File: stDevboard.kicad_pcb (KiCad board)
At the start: 4 copper layers, 50 x 100 mm, 141 parts, among them IC1 MPM3610GQV-Z, IC2 IRFR9014PBF, IC6 AT25SF041B-SSHB-B, J1 battery, J10 73412-0114, J11 USB_C_Receptacle_USB2.0_16P, J12 73412-0114, J14 Micro_SD_Card_Det2, J2 USB_C_Receptacle_USB2.0_16P, J4 Screw_Terminal_01x12, Q1 DMN3404L, Q2 DMN3404L, Q3 DMN3404L, Q4 DMN3404L, Q5 DMN3404L, Q6 MMBT2222A, Q7 MMBT2222A, Q8 DMN3404L, U1 STM32U073CCUx, U2 STM32U585CIUxQ, Y1 ECS-160-8-36B2-CKM-TR, Y2 CM7V-T1A-32.768KHZ, Y3 ECS-TXO-25CSMV-320-AM-TR, Y4 CM7V-T1A-32.768KHZ

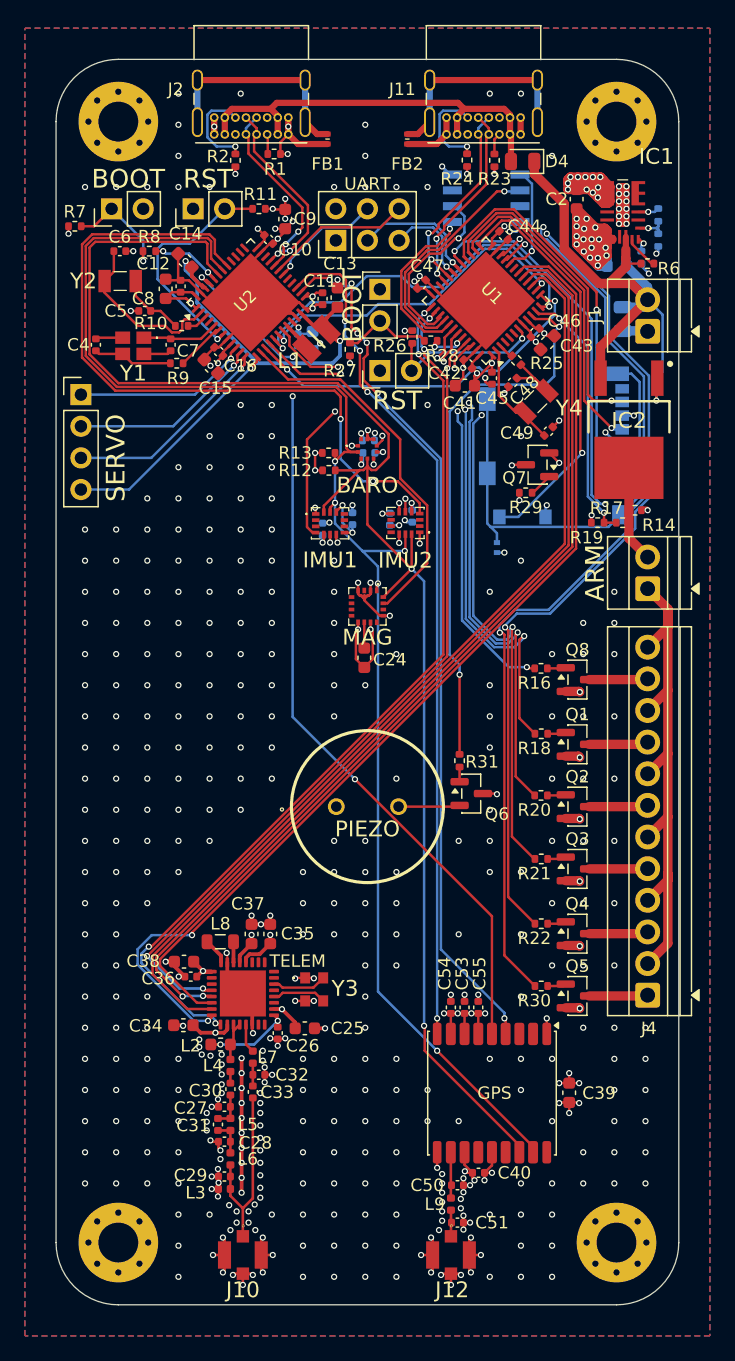
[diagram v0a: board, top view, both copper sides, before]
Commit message: schematic updated - need to redo the layout now
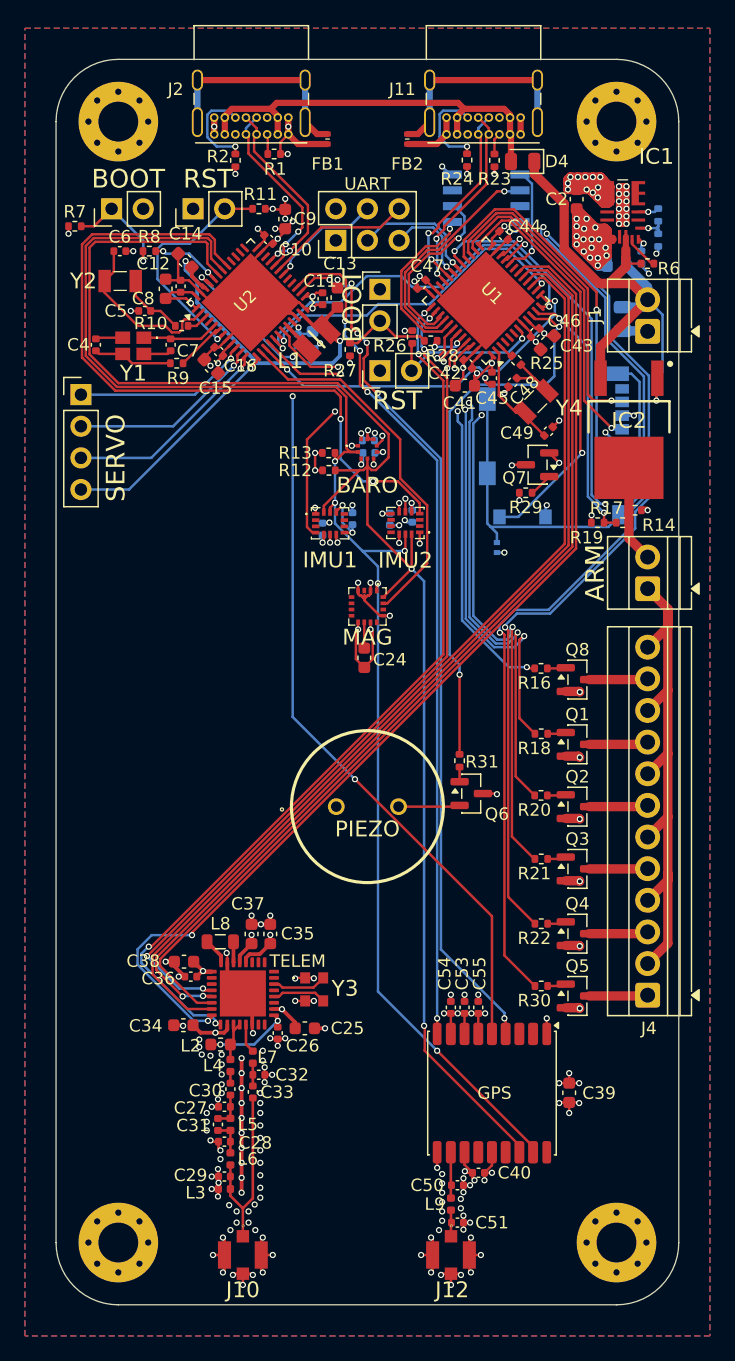
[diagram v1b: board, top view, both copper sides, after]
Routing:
- net GND: vias 471 -> 195

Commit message: started redoing layout for new pinout
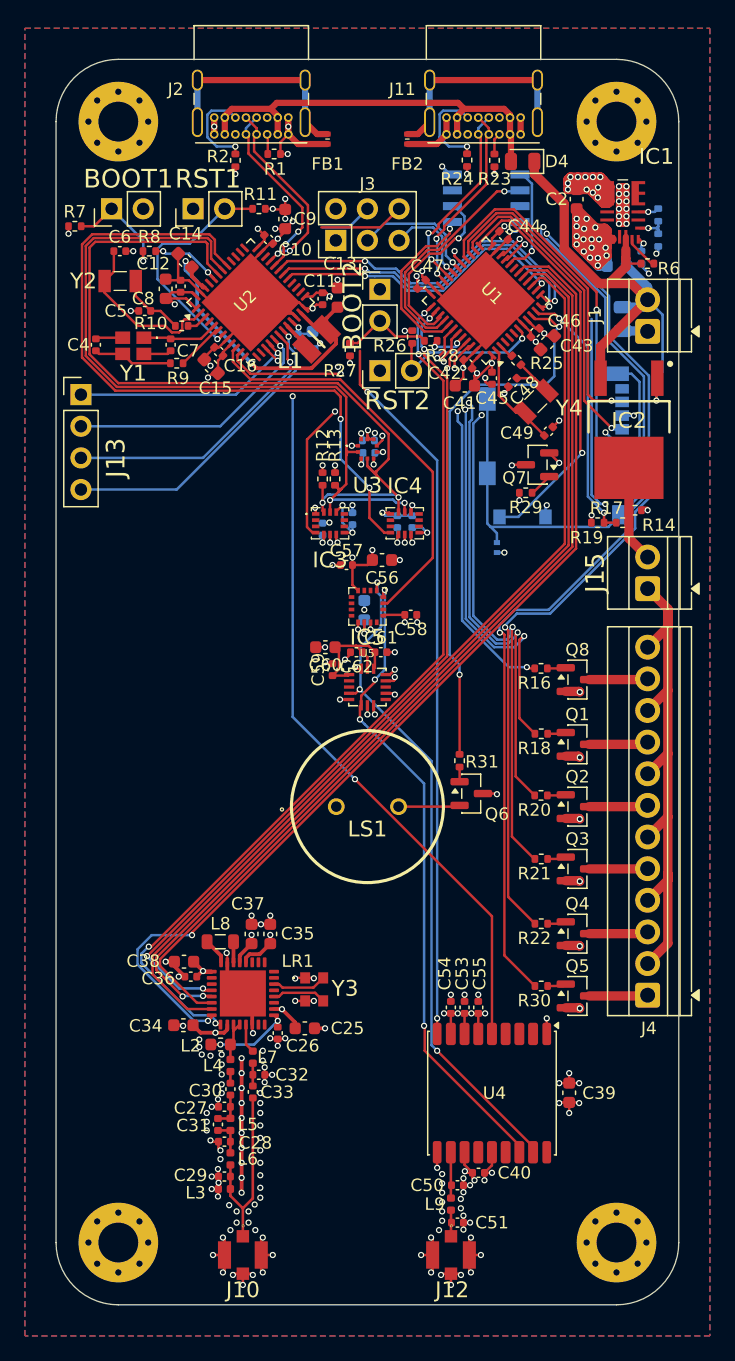
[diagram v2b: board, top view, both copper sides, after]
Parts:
- added C56: 1uF, Capacitor_SMD:C_0603_1608Metric, F.Cu at (126.2, 115.2)
- added C57: 100nF, Capacitor_SMD:C_0402_1005Metric, F.Cu at (123.3, 115.6)
- added C58: 100nF, Capacitor_SMD:C_0402_1005Metric, F.Cu at (128.5, 119.6)
- added C59: 100nF, Capacitor_SMD:C_0402_1005Metric, F.Cu at (122.2, 124.0)
- added C60: 10uF, Capacitor_SMD:C_0603_1608Metric, F.Cu at (121.6, 122.2)
- added C61: 100nF, Capacitor_SMD:C_0402_1005Metric, F.Cu at (126.1, 122.6)
- added C62: 100nF, Capacitor_SMD:C_0402_1005Metric, F.Cu at (124.1, 122.6)
- added U5: H3LIS331DLTR, footprints:QFN300X300X100-16N, F.Cu at (125.0, 125.4)
- C24: moved to B.Cu
- moved C24 3.83 mm to (124.8, 119.2), turned to 90 degrees
- moved R13 2.15 mm to (122.4, 108.7), turned to 90 degrees
- moved C23 1.81 mm to (128.6, 112.1), turned to 90 degrees
- moved C22 1.28 mm to (127.4, 112.1), turned to 90 degrees
- moved R12 0.86 mm to (121.4, 108.7), turned to 90 degrees
- moved IC4 0.06 mm to (128.0, 112.2), turned to 0 degrees
- renumbered BOOT to BOOT1, BOOT to BOOT2, IMU1 to IC3, IMU2 to IC4, MAG to IC5, SERVO to J13, ARM to J15, UART to J3, TELEM to LR1, PIEZO to LS1, RST to RST1, RST to RST2, BARO to U3, GPS to U4
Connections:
- net vr_pa renamed /rf/vr_pa
- IC5 pad 1: i2c1_sck -> i2c2_sck
- IC5 pad 16: i2c1_sda -> i2c2_sda
- U2 pad 10: /main micro/servo1 -> mag_int
- U2 pad 11: /main micro/servo2 -> bmp_int
- U2 pad 12: /main micro/servo3 -> mpu_tx_external
- U2 pad 13: /main micro/servo4 -> mpu_rx_external
- U2 pad 14: mag_int -> gps_rst
- U2 pad 15: usart_miso -> gps_int
- U2 pad 16: bmp_int -> /main micro/servo1
- U2 pad 17: usart_mosi -> /main micro/servo2
- U2 pad 18: usart_ck -> /main micro/servo3
- U2 pad 19: imu1_int1 -> /main micro/servo4
- U2 pad 26: gps_pulse -> i2c2_sck
- U2 pad 27: gps_rst -> i2c2_sda
- U2 pad 28: unconnected-(U2-PB15-Pad28) -> imu3_int1
- U2 pad 29: unconnected-(U2-PA8-Pad29) -> usart_ck
- U2 pad 30: mpu_tx_external -> usart_mosi
- U2 pad 31: mpu_rx_external -> usart_miso
- U2 pad 34: /main micro/jtms -> unconnected-(U2-PA13-Pad34)
- U2 pad 37: /main micro/jtck -> unconnected-(U2-PA14-Pad37)
- U2 pad 38: /main micro/jtdi -> unconnected-(U2-PA15-Pad38)
- U2 pad 39: /main micro/jtdo -> imu1_int1
- U2 pad 40: /main micro/njrst -> unconnected-(U2-PB4-Pad40)
- U2 pad 45: gps_int -> unconnected-(U2-PB8-Pad45)
- U4 pad 16: i2c1_sda -> i2c2_sda
- U4 pad 17: i2c1_sck -> i2c2_sck
- U4 pad 4: gps_pulse -> unconnected-(U4-TIMEPULSE-Pad4)
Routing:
- net gps_pulse: track 70.6 -> 0.00 mm, vias 6 -> 0
- net i2c1_sda: track 125.9 -> 66.6 mm
- net i2c1_sck: track 120.6 -> 63.2 mm, vias 5 -> 2
- net i2c2_sck: track 0.00 -> 54.0 mm, vias 0 -> 3
- net i2c2_sda: track 0.00 -> 51.9 mm, vias 0 -> 4
- net +3.3V: track 109.5 -> 126.0 mm, vias 59 -> 61
- net arm: track 38.8 -> 24.9 mm
- net gps_rst: track 68.3 -> 57.5 mm, vias 4 -> 2
- net gps_int: track 71.7 -> 62.6 mm, vias 4 -> 3
- net /main micro/servo3: track 16.9 -> 23.0 mm
- net /main micro/servo4: track 18.8 -> 24.8 mm
- net imu1_int1: track 20.8 -> 14.8 mm
- net mpu_tx_external: track 9.29 -> 4.21 mm, vias 1 -> 0
- net /main micro/servo2: track 15.6 -> 20.6 mm
- net mpu_rx_external: track 11.7 -> 6.86 mm
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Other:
- board text added: "${REFERENCE}"

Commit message: finished the reroute - just need to redo silkscreen and verify everything
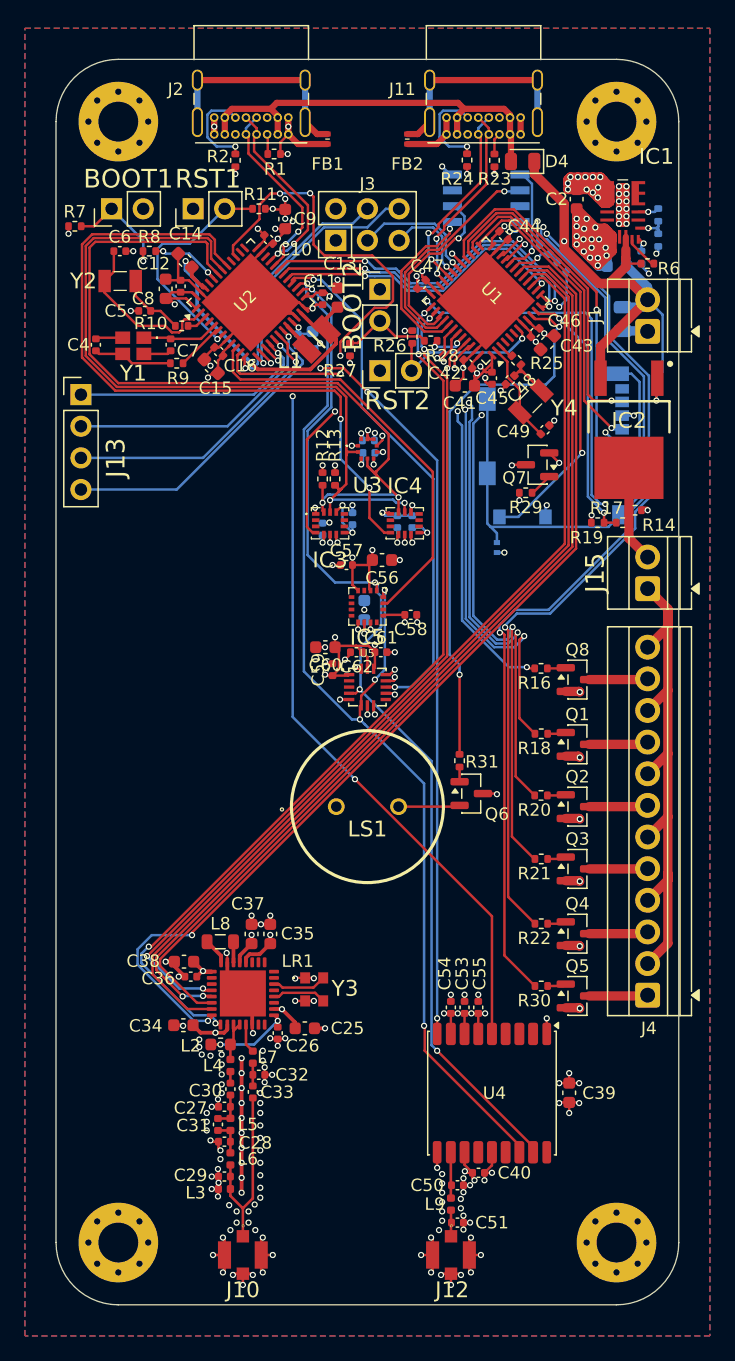
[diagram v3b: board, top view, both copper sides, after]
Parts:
- added R32: 12k, Resistor_SMD:R_0402_1005Metric, B.Cu at (140.6, 91.6)
- added R33: 3k, Resistor_SMD:R_0402_1005Metric, B.Cu at (139.2, 90.2)
- moved Y4 0.40 mm to (138.1, 102.5)
- moved C49 0.30 mm to (139.3, 104.7)
- moved C48 0.28 mm to (136.5, 100.7)
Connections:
- U1 pad 19: unconnected-(U1-PB1-Pad19) -> /peripheral micro/vbat_sense
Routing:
- net imu3_int1: track 0.00 -> 41.9 mm, vias 0 -> 2
- net i2c2_sda: track 51.9 -> 91.7 mm, vias 4 -> 5
- net imu1_int1: track 14.8 -> 45.7 mm, vias 2 -> 4
- net i2c2_sck: track 54.0 -> 84.3 mm, vias 3 -> 4
- net arm: track 24.9 -> 43.3 mm, vias 3 -> 4
- net mpu_tx_external: track 4.21 -> 19.6 mm, vias 0 -> 1
- net mpu_rx_external: track 6.86 -> 20.4 mm, vias 0 -> 1
- net gps_rst: track 57.5 -> 66.1 mm, vias 2 -> 4
- net +BATT: track 43.1 -> 51.6 mm, vias 0 -> 2
- net +3.3V: track 126.0 -> 131.7 mm, vias 61 -> 64
- net GND: track 234.6 -> 238.9 mm, vias 206 -> 207
- net /peripheral micro/vbat_sense: track 0.00 -> 4.28 mm, vias 0 -> 1
- net Net-(C48-Pad2): track 5.75 -> 4.27 mm
- net /main micro/servo1: track 18.2 -> 19.5 mm
- net Net-(U1-PC13): track 8.83 -> 8.16 mm
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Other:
- board text added: "IC5"
- board text removed: "${REFERENCE}"
